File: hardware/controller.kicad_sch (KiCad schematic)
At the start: 41 parts, among them J1 Connector, USB-TYPE-C-16P, J2 AXK6F20347YG, J3 AFA01-S08FCA-00, U1 ESP32-C6-WROOM-1, U2 BQ24074RGTR, U3 TLA2518IRTER, U6 TPS62142RGTR

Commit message: :sparkles: finish all hardware designs
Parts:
- added R13: 100Ω, KeysDock:R_0402, symbol components:0402,100Ω
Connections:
- net at STAT1.L2 (DI): now also R13.2; no longer U1.20 (GPIO22)
- new net: R13.1, U1.20 (GPIO22)
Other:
- moved on the sheet: STAT1

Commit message: :sparkles: assembly all the part!
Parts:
- J1: footprint KeysDock:TYPE-C-SMD_HX-TYPE-C-16PIN -> KeysDock:HC-TYPE-C-16P-CB1.6; symbol components:Connector, USB-TYPE-C-16P -> components:HC-TYPE-C-16P-CB1.6

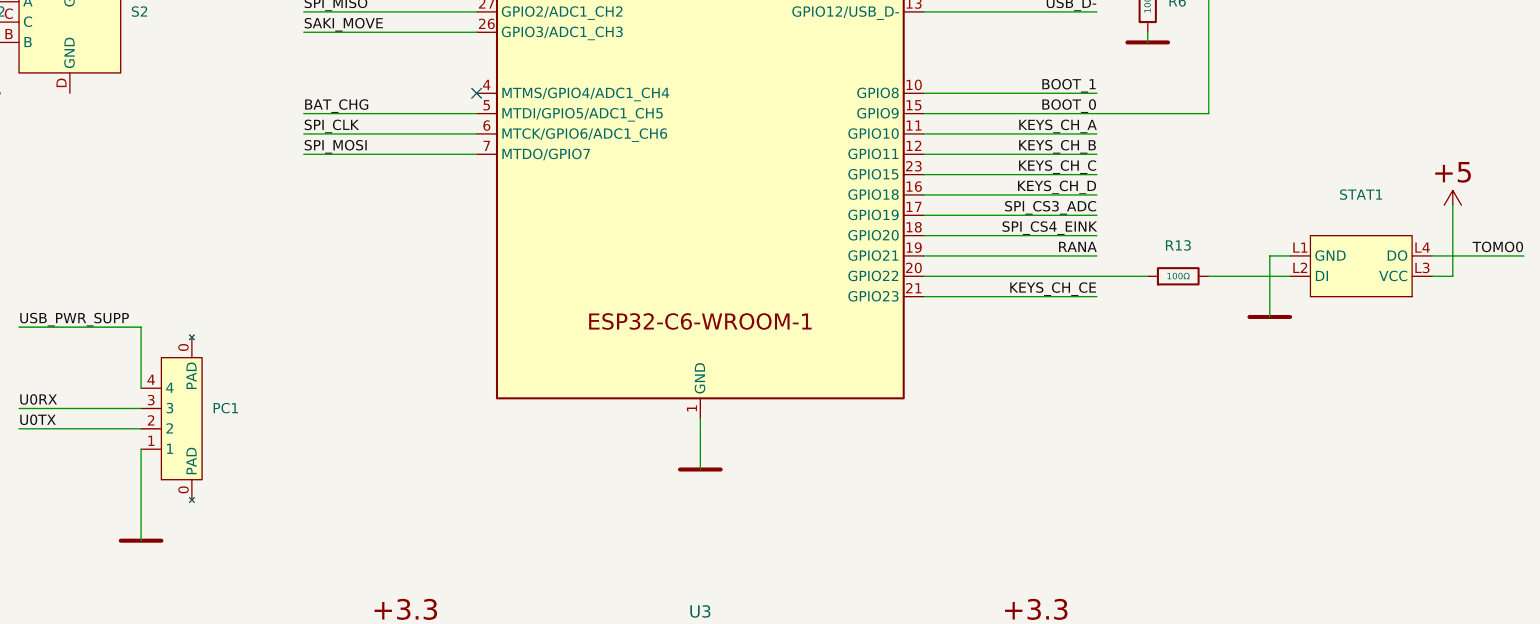
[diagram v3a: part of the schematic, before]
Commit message: :art: improve LED positions
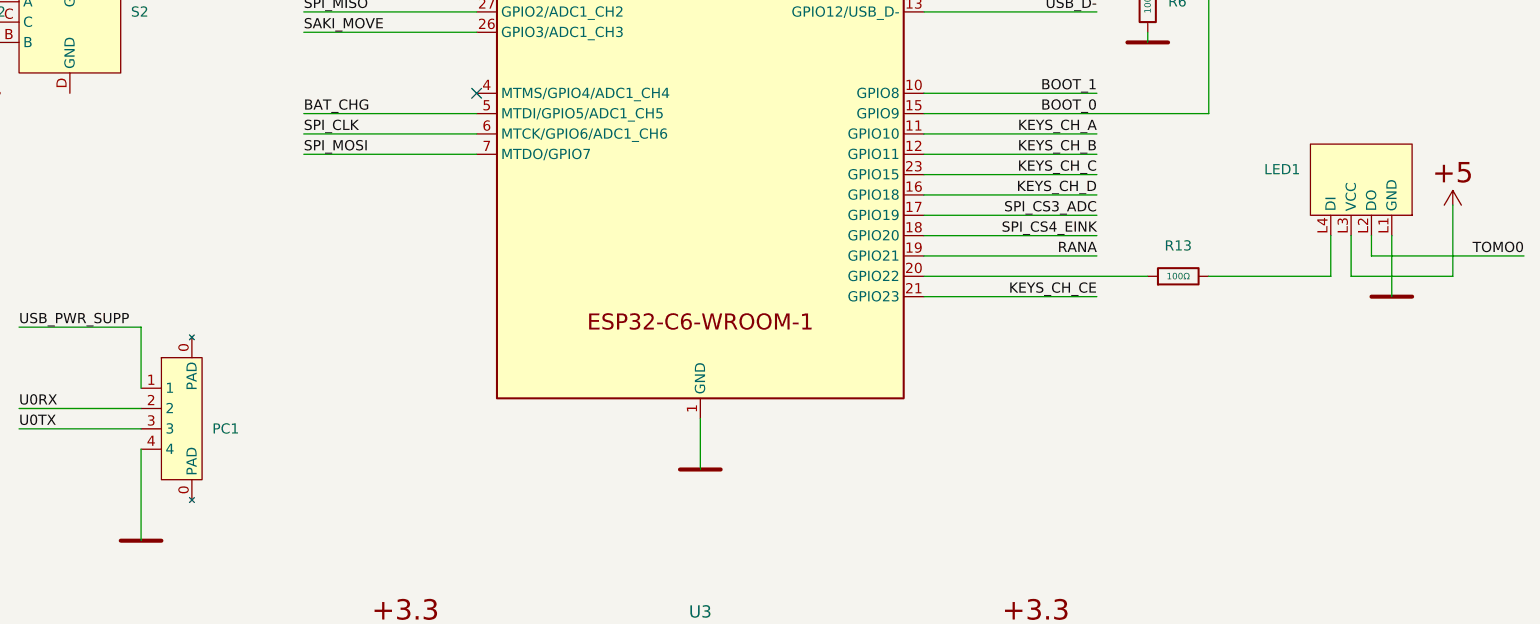
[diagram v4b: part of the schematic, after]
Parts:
- removed STAT1: ~, KeysDock:XL-3528RGBW-WS2812B, symbol components:XL-3528RGBW-WS2812B
- added LED1: ~, KeysDock:XL-3512RGBW-WS2812B, symbol components:XL-3512RGBW-WS2812B
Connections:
- net P,+5: now also LED1.L3 (VCC)
- net P,E: now also PC1.4, LED1.L1 (GND); no longer PC1.1
- net TOMO0: now also LED1.L2 (DO)
- net U0RX: now also PC1.2; no longer PC1.3
- net U0TX: now also PC1.3; no longer PC1.2
- net USB_PWR_SUPP: now also PC1.1; no longer PC1.4
- net at R13.2: now also LED1.L4 (DI)
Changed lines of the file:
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@@
 	(title_block
 		(title "Keys Dock Controller")
-		(date "2025-12-14")
-		(rev "0.2.6")
+		(date "2026-01-06")
+		(rev "0.2.7")
 		(company "keys.woooo.tech")
 	)
@@
 	(wire
 		(pts
-			(xy 355.6 99.06) (xy 365.76 99.06)
+			(xy 375.92 93.98) (xy 375.92 96.52)
+		)
+		(stroke
+			(width 0)
+			(type default)
+		)
+	)
+	(wire
+		(pts
+			(xy 355.6 99.06) (xy 370.84 99.06)
 		)
 		(stroke
@@
 	(wire
 		(pts
+			(xy 375.92 96.52) (xy 394.97 96.52)
+		)
+		(stroke
+			(width 0)
+			(type default)
+		)
+	)
+	(wire
+		(pts
 			(xy 161.29 102.87) (xy 171.45 102.87)
 		)
@@
 	(wire
 		(pts
+			(xy 373.38 93.98) (xy 373.38 99.06)
+		)
+		(stroke
+			(width 0)
+			(type default)
+		)
+	)
+	(wire
+		(pts
 			(xy 165.1 196.85) (xy 165.1 204.47)
 		)
@@
 	(wire
 		(pts
+			(xy 373.38 99.06) (xy 386.08 99.06)
+		)
+		(stroke
+			(width 0)
+			(type default)
+		)
+	)
+	(wire
+		(pts
 			(xy 203.2 148.59) (xy 185.42 148.59)
 		)
@@
 	(wire
 		(pts
+			(xy 370.84 99.06) (xy 370.84 93.98)
+		)
+		(stroke
+			(width 0)
+			(type default)
+		)
+	)
+	(wire
+		(pts
 			(xy 320.04 93.98) (xy 341.63 93.98)
 		)
@@
 	(wire
 		(pts
-			(xy 365.76 96.52) (xy 363.22 96.52)
-		)
-		(stroke
-			(width 0)
-			(type default)
-		)
-	)
-	(wire
-		(pts
 			(xy 102.87 127) (xy 102.87 132.08)
 		)
@@
 	(wire
 		(pts
-			(xy 383.54 99.06) (xy 386.08 99.06)
-		)
-		(stroke
-			(width 0)
-			(type default)
-		)
-	)
-	(wire
-		(pts
 			(xy 102.87 132.08) (xy 102.87 134.62)
 		)
@@
 	(wire
 		(pts
-			(xy 363.22 96.52) (xy 363.22 104.14)
+			(xy 378.46 93.98) (xy 378.46 101.6)
 		)
 		(stroke
@@
 	(wire
 		(pts
-			(xy 383.54 96.52) (xy 394.97 96.52)
-		)
-		(stroke
-			(width 0)
-			(type default)
-		)
-	)
-	(wire
-		(pts
 			(xy 99.06 200.66) (xy 106.68 200.66)
 		)
@@
 	)
 	(symbol
-		(lib_id "components:XL-3528RGBW-WS2812B")
-		(at 374.65 97.79 180)
-		(unit 1)
-		(exclude_from_sim no)
-		(in_bom yes)
-		(on_board yes)
-		(dnp no)
-		(fields_autoplaced yes)
-		(property "Reference" "STAT1"
-			(at 374.65 88.9 0)
-			(effects
-				(font
-					(size 1.27 1.27)
-				)
-			)
-		)
-		(property "Value" "~"
-			(at 374.65 91.44 0)
-			(effects
-				(font
-					(size 1.27 1.27)
-				)
-			)
-		)
-		(property "Footprint" "KeysDock:XL-3528RGBW-WS2812B"
-			(at 374.65 97.79 0)
-			(effects
-				(font
-					(size 1.27 1.27)
-				)
-				(hide yes)
-			)
-		)
-		(property "Datasheet" "${KIPRJMOD}/docs/xl-3528rgbw-2812b.pdf"
-			(at 374.65 97.79 0)
-			(effects
-				(font
-					(size 1.27 1.27)
-				)
-				(hide yes)
-			)
-		)
-		(property "Description" ""
-			(at 374.65 97.79 0)
-			(effects
-				(font
-					(size 1.27 1.27)
-				)
-				(hide yes)
-			)
-		)
-		(pin "L4"
-		)
-		(pin "L3"
-		)
-		(pin "L1"
-		)
-		(pin "L2"
-		)
-		(instances
-			(project ""
-				(path "/5e396643-4ddf-447c-ad2b-abd8fc998127/bc34e183-172c-409f-bcd2-a6a538b3704f"
-					(reference "STAT1")
-					(unit 1)
-				)
-			)
-			(project ""
-				(path "/a4e7072d-1db6-48c9-937c-096c1ce61d37"
-					(reference "STAT1")
-					(unit 1)
-				)
-			)
-		)
-	)
-	(symbol
 		(lib_id "components:HC-TYPE-C-16P-CB1.6")
 		(at 82.55 36.83 270)
@@
 	(symbol
 		(lib_id "PCM_Generic:P,0")
-		(at 363.22 104.14 0)
+		(at 378.46 101.6 0)
 		(unit 1)
 		(exclude_from_sim no)
@@
 		(fields_autoplaced yes)
 		(property "Reference" "#PWR021"
-			(at 367.03 100.33 0)
+			(at 382.27 97.79 0)
 			(effects
 				(font
@@
 		)
 		(property "Value" "P,E"
-			(at 367.03 104.14 0)
+			(at 382.27 101.6 0)
 			(effects
 				(font
@@
 		)
 		(property "Footprint" ""
-			(at 363.22 104.14 0)
+			(at 378.46 101.6 0)
 			(effects
 				(font
@@
 		)
 		(property "Datasheet" ""
-			(at 363.22 104.14 0)
+			(at 378.46 101.6 0)
 			(effects
 				(font
@@
 		)
 		(property "Description" "global node 0; simplified functional (equipotential) bonding (FB); simplified frame/chassis"
-			(at 363.22 104.14 0)
+			(at 378.46 101.6 0)
 			(effects
 				(font
@@
 		(lib_id "components:HC-1.25-4PWT")
 		(at 227.33 116.84 90)
+		(mirror x)
 		(unit 1)
 		(exclude_from_sim no)
@@
 		(on_board yes)
 		(dnp no)
-		(fields_autoplaced yes)
 		(property "Reference" "PC1"
-			(at 231.14 115.5699 90)
+			(at 231.14 118.1101 90)
 			(effects
 				(font
@@
 		)
 		(property "Value" "~"
-			(at 231.14 118.1099 90)
+			(at 231.14 115.5701 90)
 			(effects
 				(font
@@
 					(unit 1)
 				)
+			)
+		)
+	)
+	(symbol
+		(lib_id "components:XL-3512RGBW-WS2812B")
+		(at 374.65 86.36 270)
+		(mirror x)
+		(unit 1)
+		(exclude_from_sim no)
+		(in_bom yes)
+		(on_board yes)
+		(dnp no)
+		(property "Reference" "LED1"
+			(at 367.03 85.7249 90)
+			(effects
+				(font
+					(size 1.27 1.27)
+				)
+				(justify right)
+			)
+		)
+		(property "Value" "~"
+			(at 367.03 88.2649 90)
+			(effects
+				(font
+					(size 1.27 1.27)
+				)
+				(justify right)
+			)
+		)
+		(property "Footprint" "KeysDock:XL-3512RGBW-WS2812B"
+			(at 374.65 86.36 0)
+			(effects
+				(font
+					(size 1.27 1.27)
+				)
+				(hide yes)
+			)
+		)
+		(property "Datasheet" "kicad-embed://xl-3528rgbw-2812b.pdf"
+			(at 374.65 86.36 0)
+			(effects
+				(font
+					(size 1.27 1.27)
+				)
+				(hide yes)
+			)
+		)
+		(property "Description" ""
+			(at 374.65 86.36 0)
+			(effects
+				(font
+					(size 1.27 1.27)
+				)
+				(hide yes)
+			)
+		)
+		(pin "L4"
+		)
+		(pin "L3"
+		)
+		(pin "L1"
+		)
+		(pin "L2"
+		)
+		(instances
+			(project ""
+				(path "/a4e7072d-1db6-48c9-937c-096c1ce61d37"
+					(reference "LED1")
+					(unit 1)
+				)

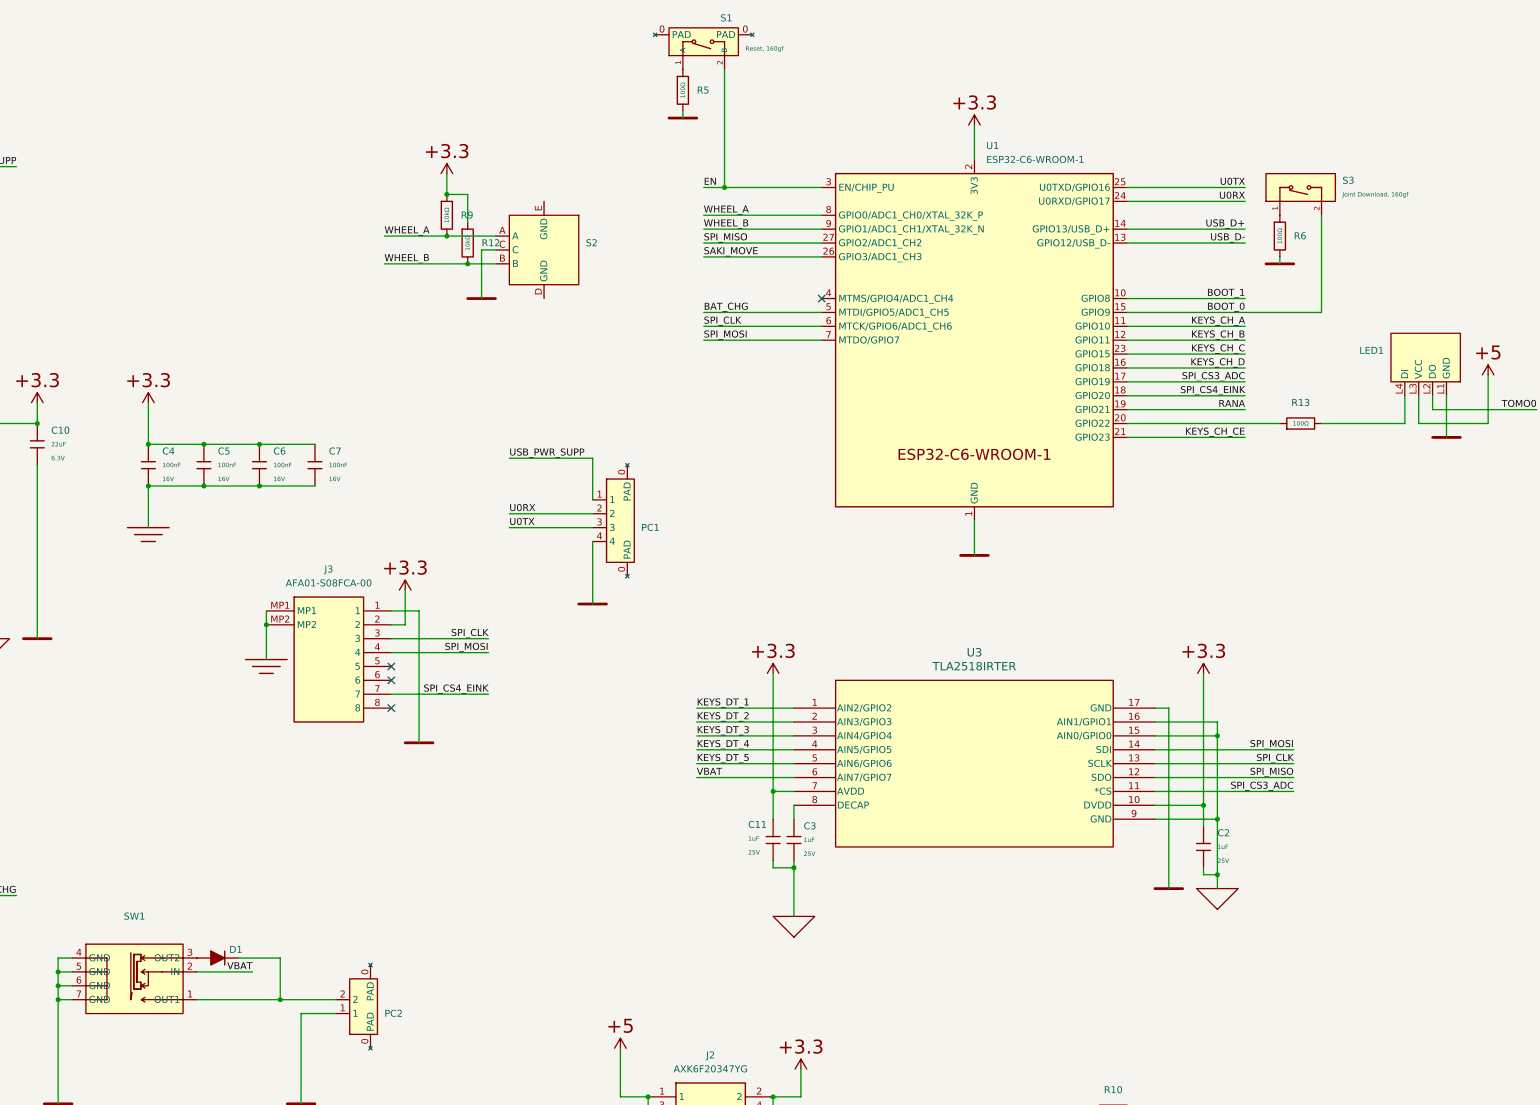
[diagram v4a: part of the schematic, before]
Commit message: :sparkles: add bom table
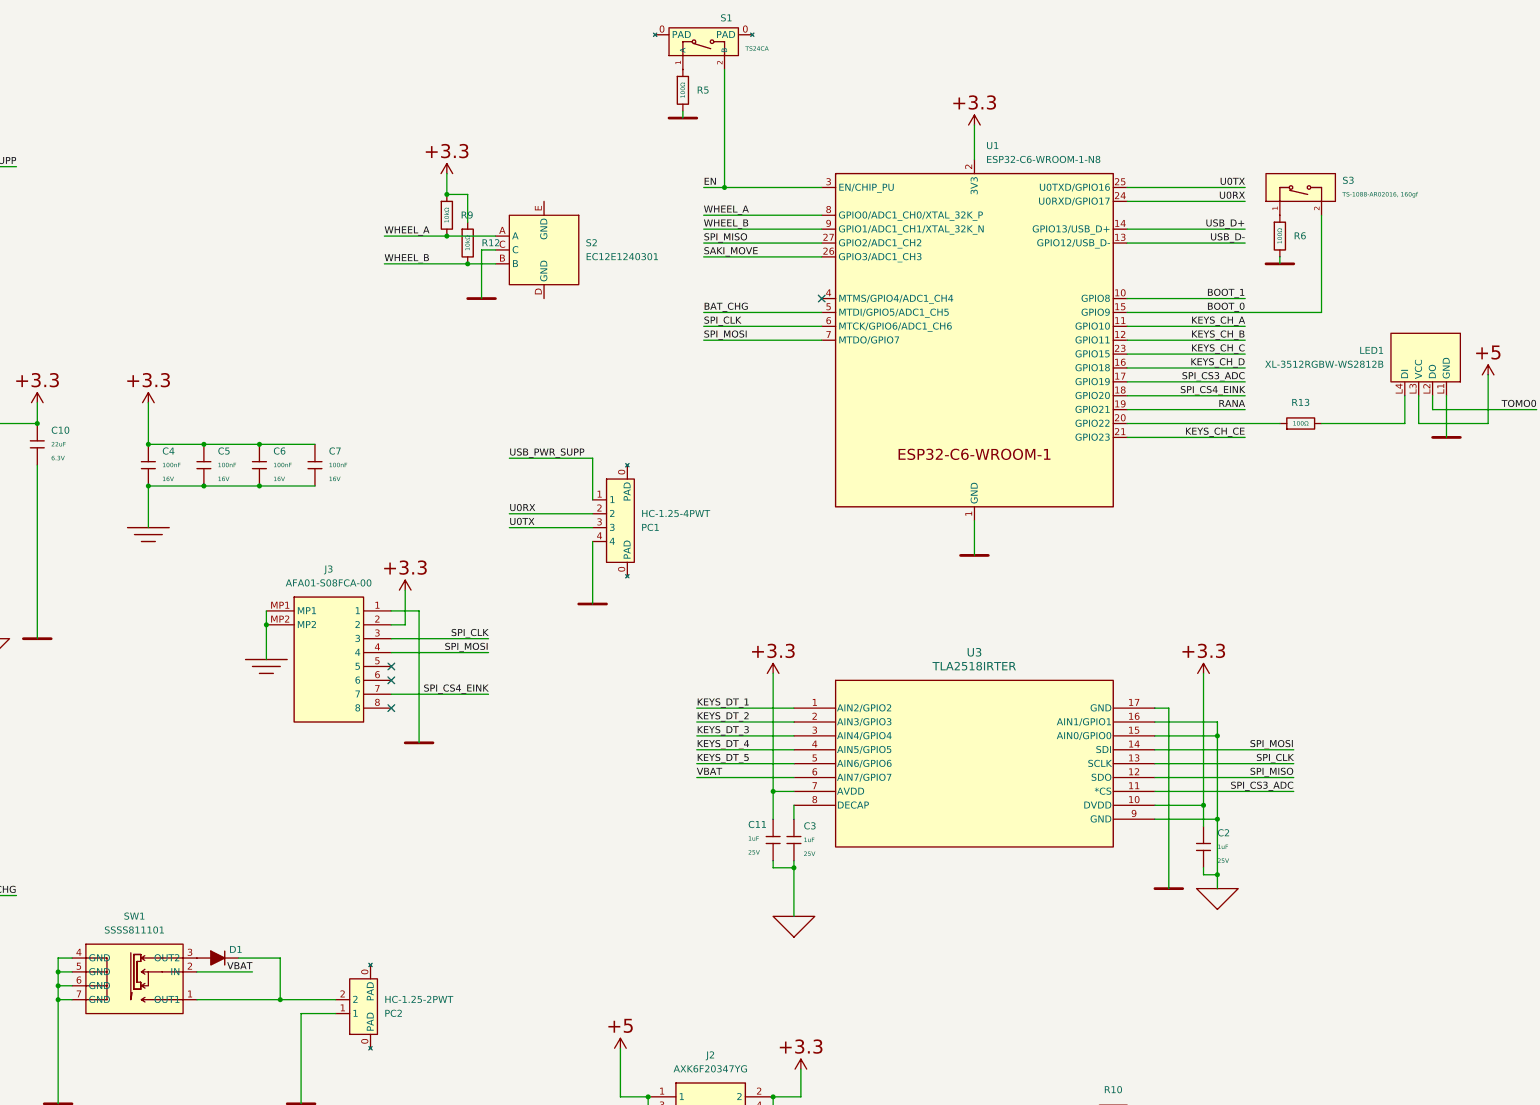
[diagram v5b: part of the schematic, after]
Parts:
- D1: LCSC (none) -> C78741; Manufacturer (none) -> MCC(美微科)
- J1: value Connector, USB-TYPE-C-16P -> HC-TYPE-C-16P-CB1.6; LCSC C2927039 -> C2894902; Manufacturer (none) -> HCTL(华灿天禄)
- J2: LCSC (none) -> C559781; Manufacturer (none) -> Panasonic; PartNumber (none) -> AXK6F20347YG
- J3: LCSC (none) -> C262755; Manufacturer (none) -> JUSHUO; PartNumber (none) -> AFA01-S08FCA-00
- LED1: value ~ -> XL-3512RGBW-WS2812B; LCSC (none) -> C49237874; Manufacturer (none) -> XINGLIGHT(成兴光)
- PC1: value ~ -> HC-1.25-4PWT; LCSC (none) -> C2845381; Manufacturer (none) -> HCTL(华灿天禄)
- PC2: value ~ -> HC-1.25-2PWT; LCSC (none) -> C2845379; Manufacturer (none) -> HCTL(华灿天禄)
- S1: value Reset, 160gf -> TS24CA; LCSC C720477 -> C393942; Manufacturer XUNPU -> SHOU HAN(首韩)
- S2: value ~ -> EC12E1240301; LCSC (none) -> C351235; Manufacturer (none) -> ALPSALPINE
- S3: value Joint Download, 160gf -> TS-1088-AR02016, 160gf
- SW1: value ~ -> SSSS811101; LCSC (none) -> C109335; Manufacturer (none) -> ALPSALPINE
- U1: value ESP32-C6-WROOM-1 -> ESP32-C6-WROOM-1-N8; Manufacturer (none) -> Espressif Systems
- U2: Height (none) -> 1mm; LCSC (none) -> C54313; Manufacturer (none) -> Texas Instruments; Standard (none) -> IPC 7351B
- U3: LCSC (none) -> C1855741; Manufacturer (none) -> Texas Instruments
- U6: LCSC (none) -> C129331; Manufacturer (none) -> Texas Instruments

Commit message: :bug: improve hardware design
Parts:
- added C12: 1uF, KeysDock:C_0402, symbol components:0402,1uF
- added C13: 100nF, KeysDock:C_0402, symbol components:0402,100nF
- added R14, R15, R16, R18: 10kΩ, KeysDock:R_0402, symbol components:0402,10kΩ
- added R17, R19, R20, R21: 100kΩ, KeysDock:R_0402, symbol components:0402,100kΩ
- added R22, R23: 22Ω, KeysDock:R_0402, symbol components:0402,22Ω
- added R24: 47kΩ, KeysDock:R_0402, symbol components:0402,47kΩ
- R2, R4: value 4.7kΩ -> 5.1kΩ; symbol components:0402,4.7kΩ -> components:0402,5.1kΩ; LCSC C25900 -> C25941; Part 0402WGF4701TCE -> 0402WGJ0512TCE; Resistance 4.7kΩ -> 5.1kΩ
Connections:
- net BAT_CHG: now also R17.2
- net BOOT_0: now also R16.2
- net BOOT_1: now also R15.2
- net EN: now also C12.1, R14.2
- net P,+3.3: now also R14.1, R15.1, R16.1, R17.1, R18.1
- net P,E: now also C12.2, R19.2, R24.1; no longer U2.14 (TMR)
- net P,GND: now also C13.2, R21.1
- net RANA: now also R19.1
- net SAKI_MOVE: now also R18.2
- net USB_D+: now also R22.2; no longer J1.A6 (D+), J1.B6 (D+)
- net USB_D-: now also R23.2; no longer J1.A7 (D-), J1.B7 (D-)
- net VBAT: now also R20.1; no longer U3.6 (AIN7/GPIO7)
- net BAT_PGOOD: now reaches U2.7 (~{PGOOD})
- net BAT_PGOOD: now also U1.4 (MTMS/GPIO4/ADC1_CH4)
- new net: C13.1, R20.2, R21.2, U3.6 (AIN7/GPIO7)
- new net: R24.2, U2.14 (TMR)
- new net: J1.A6 (D+), J1.B6 (D+), R22.1
- new net: J1.A7 (D-), J1.B7 (D-), R23.1
- no-connect marks 5 -> 3
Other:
- moved on the sheet: J3, R12, R13, R6, R9, S2, S3
